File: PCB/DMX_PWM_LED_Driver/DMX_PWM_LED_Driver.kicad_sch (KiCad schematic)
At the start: 40 parts, among them J1 Programming_Header, J2 PWR_OUT, J3 PWR_IN, J4 LED_OUT, J5 Conn_Left, J6 Conn_Right, Q1 IRLZ44N, SW1 SW_SPST, SW2 SW_DIP_x04, U2 MAX485E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

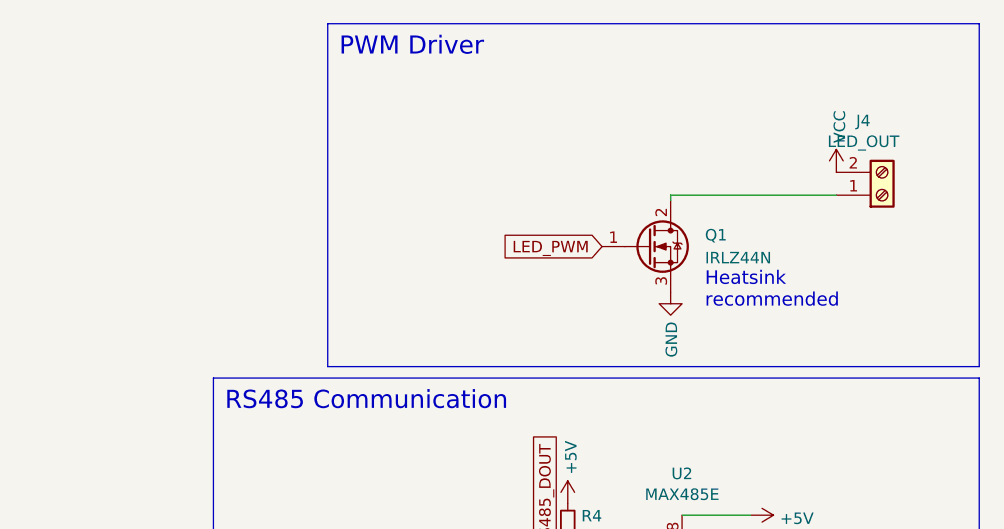
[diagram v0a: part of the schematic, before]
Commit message: Updated design of PWM board and code updated for slave boards
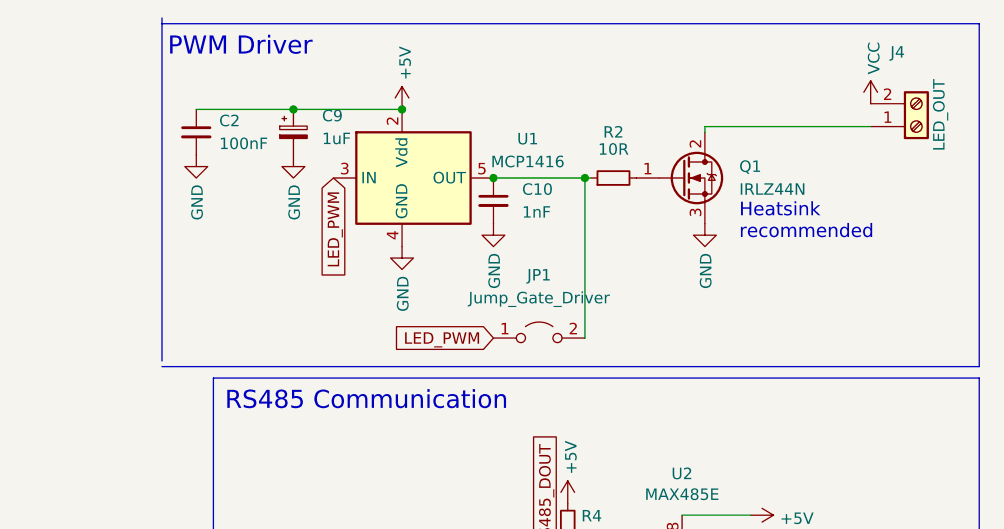
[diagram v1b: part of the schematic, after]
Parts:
- added C10: 1nF, Capacitor_SMD:C_0603_1608Metric, symbol Device:C_Small
- added C2: 100nF, Capacitor_SMD:C_0805_2012Metric, symbol Device:C_Small
- added C9: 1uF, Capacitor_THT:CP_Radial_D5.0mm_P2.00mm, symbol Device:C_Polarized_Small
- added JP1: Jump_Gate_Driver, Jumper:SolderJumper-2_P1.3mm_Open_Pad1.0x1.5mm, symbol Jumper:Jumper_2_Open
- added R2: 10R, Resistor_SMD:R_0805_2012Metric, symbol Device:R_Small
- added U1: MCP1416, Package_TO_SOT_SMD:SOT-23-5, symbol Driver_FET:MCP1416
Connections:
- net +5V: now also C2.1, C9.1, U1.2 (Vdd)
- net GND: now also C10.2, C2.2, C9.2, U1.4 (GND)
- net LED_PWM: now also JP1.1 (A), U1.3 (IN); no longer Q1.1 (G)
- new net: C10.1, JP1.2 (B), R2.1, U1.5 (OUT)
- new net: Q1.1 (G), R2.2
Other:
- moved on the sheet: J4, Q1
